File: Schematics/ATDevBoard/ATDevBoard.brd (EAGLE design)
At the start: 67.7 x 54.4 mm, 39 parts, among them U1 TINY85-DIP

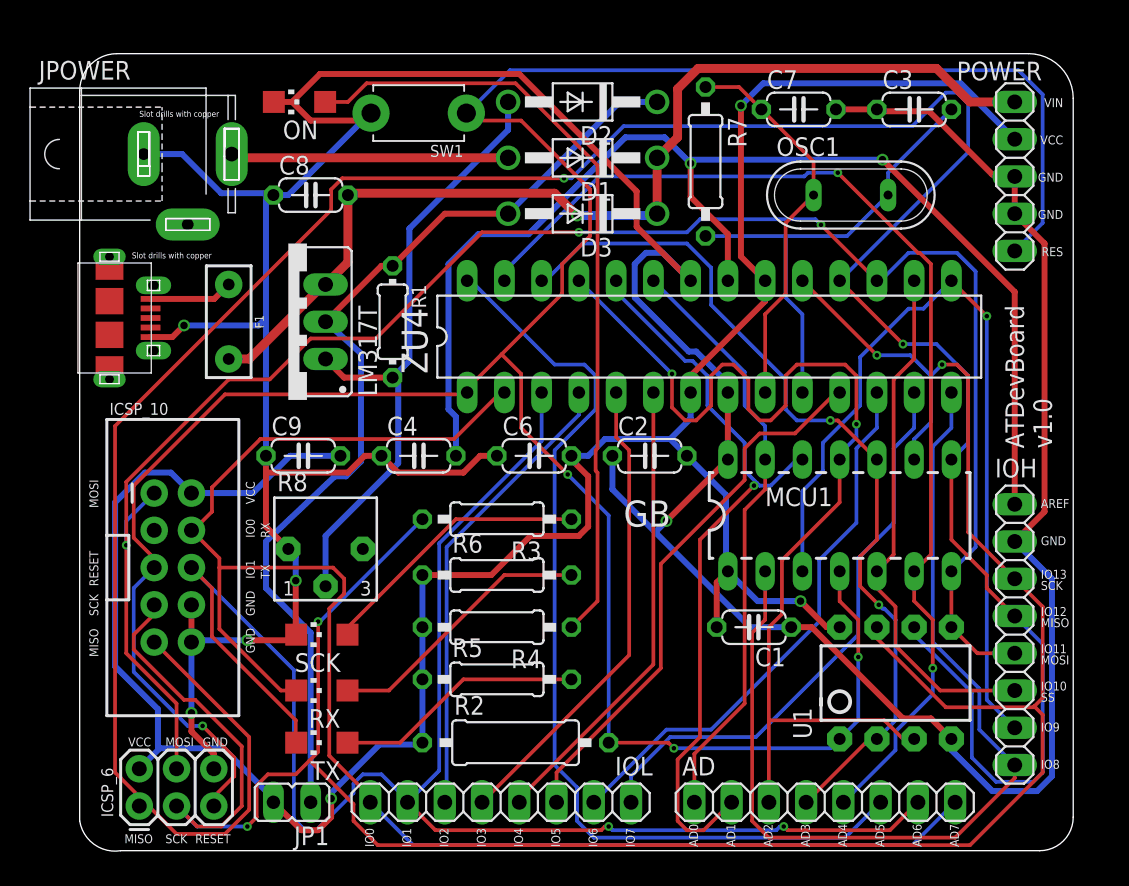
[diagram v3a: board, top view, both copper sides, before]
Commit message: Added fist version of gerber file for SeeedStudio
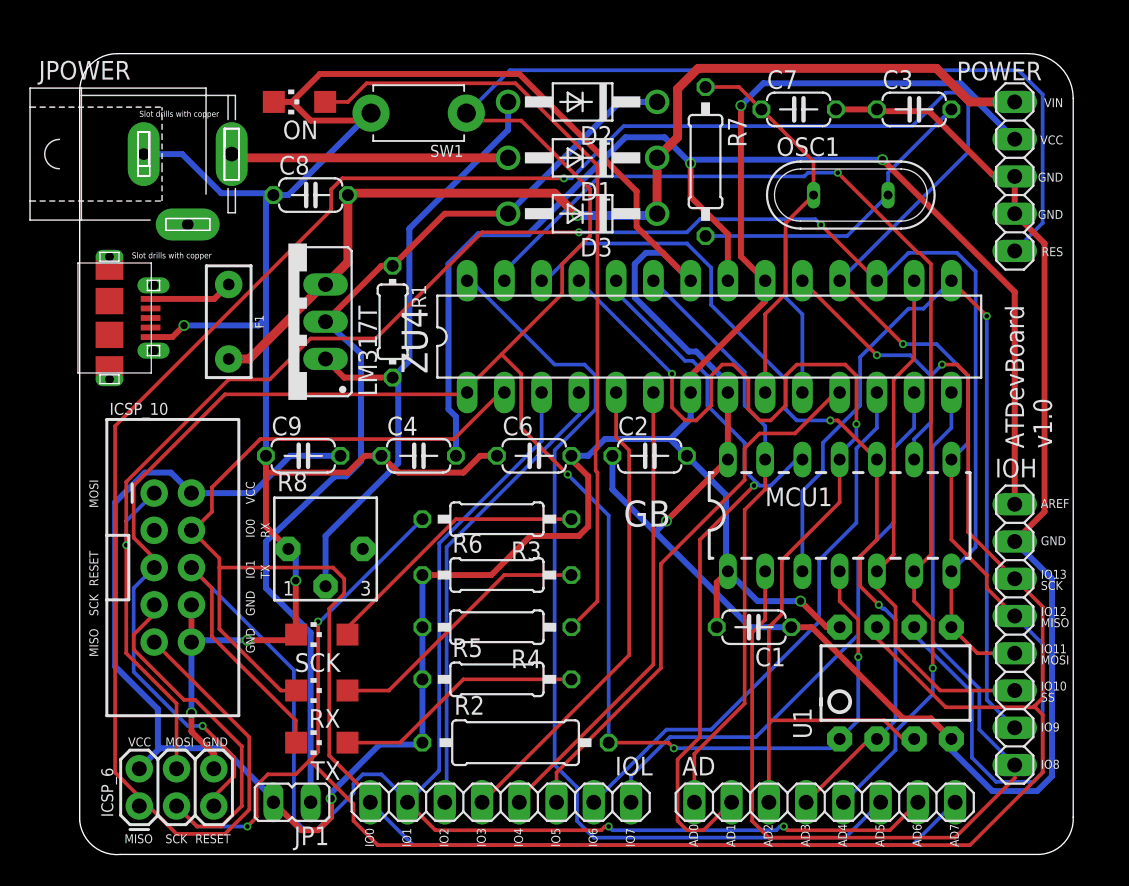
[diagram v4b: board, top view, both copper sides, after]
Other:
- board size 67.7 x 54.4 mm -> 67.7 x 54.6 mm
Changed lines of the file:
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@@
 <plain>
 <wire x1="-0.254" y1="51.298" x2="-0.254" y2="1.524" width="0" layer="20"/>
-<wire x1="-0.254" y1="1.524" x2="2.54" y2="-0.508" width="0" layer="20" curve="90"/>
-<wire x1="2.54" y1="-0.508" x2="65.202" y2="-0.508" width="0" layer="20"/>
-<wire x1="65.202" y1="-0.508" x2="67.488" y2="1.778" width="0" layer="20" curve="90"/>
+<wire x1="-0.254" y1="1.524" x2="2.54" y2="-0.762" width="0" layer="20" curve="90"/>
+<wire x1="2.54" y1="-0.762" x2="65.202" y2="-0.762" width="0" layer="20"/>
+<wire x1="65.202" y1="-0.762" x2="67.488" y2="1.778" width="0" layer="20" curve="90"/>
 <wire x1="67.488" y1="1.778" x2="67.488" y2="50.786046875" width="0" layer="20"/>
 <wire x1="67.488" y1="50.786046875" x2="64.436046875" y2="53.838" width="0" layer="20" curve="90"/>
@@
 </class>
 </classes>
-<designrules name="SeeedStudio_2layer_DRU_no_angle_20140221">
-<description language="de">&lt;b&gt;EAGLE Design Rules&lt;/b&gt;
+<designrules name="oshpark-2layer">
+<description language="en">&lt;b&gt;OSH Park Design Rules&lt;/b&gt;
 &lt;p&gt;
-Die Standard-Design-Rules sind so gewählt, dass sie für
-die meisten Anwendungen passen. Sollte ihre Platine
-besondere Anforderungen haben, treffen Sie die erforderlichen
-Einstellungen hier und speichern die Design Rules unter
-einem neuen Namen ab.</description>
-<description language="en">&lt;b&gt;EAGLE Design Rules&lt;/b&gt;
+Please make sure your boards conform to these design rules.
+&lt;/p&gt;
 &lt;p&gt;
-The default Design Rules have been set to cover
-a wide range of applications. Your particular design
-may have different requirements, so please make the
-necessary adjustments and save your customized
-design rules under a new name.</description>
-<description language="zh">&lt;b&gt;Seeed Studio EAGLE Design Rules&lt;/b&gt;
-</description>
+Note, that not all DRC settings must be set by the manufacturer. Several can be adjusted for the design, including those listed on our docs page here.
+&lt;a href=&quot;http://docs.oshpark.com/design-tools/eagle/design-rules-files/&quot;&gt;Adjustable Settings&lt;/a&gt;
+&lt;/p&gt;</description>
 <param name="layerSetup" value="(1*16)"/>
-<param name="mtCopper" value="0.035mm 0.0175mm 0.035mm 0.035mm 0.035mm 0.035mm 0.035mm 0.035mm 0.035mm 0.035mm 0.035mm 0.035mm 0.035mm 0.035mm 0.0175mm 0.035mm"/>
-<param name="mtIsolate" value="1.5mm 1.1mm 0.2mm 0.15mm 0.2mm 0.15mm 0.2mm 0.15mm 0.2mm 0.15mm 0.2mm 0.15mm 0.2mm 0.15mm 0.2mm"/>
+<param name="mtCopper" value="0.035559375mm 0.0356mm 0.0356mm 0.0356mm 0.0356mm 0.0356mm 0.0356mm 0.0356mm 0.0356mm 0.0356mm 0.0356mm 0.0356mm 0.0356mm 0.0356mm 0.0356mm 0.035559375mm"/>
+<param name="mtIsolate" value="1.6mm 0.1499mm 0.2007mm 0.1499mm 0.2007mm 0.1499mm 0.2007mm 0.1499mm 0.2007mm 0.1499mm 0.2007mm 0.1499mm 0.2007mm 0.1499mm 0.2007mm"/>
 <param name="mdWireWire" value="6mil"/>
 <param name="mdWirePad" value="6mil"/>
@@
 <param name="mdPadVia" value="6mil"/>
 <param name="mdViaVia" value="6mil"/>
-<param name="mdSmdPad" value="0mil"/>
-<param name="mdSmdVia" value="0mil"/>
-<param name="mdSmdSmd" value="0mil"/>
+<param name="mdSmdPad" value="6mil"/>
+<param name="mdSmdVia" value="6mil"/>
+<param name="mdSmdSmd" value="6mil"/>
 <param name="mdViaViaSameLayer" value="8mil"/>
 <param name="mnLayersViaInSmd" value="2"/>
-<param name="mdCopperDimension" value="10mil"/>
-<param name="mdDrill" value="10mil"/>
+<param name="mdCopperDimension" value="15mil"/>
+<param name="mdDrill" value="6mil"/>
 <param name="mdSmdStop" value="0mil"/>
 <param name="msWidth" value="6mil"/>
-<param name="msDrill" value="12mil"/>
-<param name="msMicroVia" value="12mil"/>
+<param name="msDrill" value="10mil"/>
+<param name="msMicroVia" value="10mil"/>
 <param name="msBlindViaRatio" value="0.5"/>
 <param name="rvPadTop" value="0.25"/>
@@
 <param name="rvMicroViaOuter" value="0.25"/>
 <param name="rvMicroViaInner" value="0.25"/>
-<param name="rlMinPadTop" value="10mil"/>
+<param name="rlMinPadTop" value="5mil"/>
 <param name="rlMaxPadTop" value="20mil"/>
-<param name="rlMinPadInner" value="10mil"/>
+<param name="rlMinPadInner" value="5mil"/>
 <param name="rlMaxPadInner" value="20mil"/>
-<param name="rlMinPadBottom" value="10mil"/>
+<param name="rlMinPadBottom" value="5mil"/>
 <param name="rlMaxPadBottom" value="20mil"/>
-<param name="rlMinViaOuter" value="6mil"/>
+<param name="rlMinViaOuter" value="5mil"/>
 <param name="rlMaxViaOuter" value="20mil"/>
-<param name="rlMinViaInner" value="6mil"/>
+<param name="rlMinViaInner" value="5mil"/>
 <param name="rlMaxViaInner" value="20mil"/>
-<param name="rlMinMicroViaOuter" value="4mil"/>
+<param name="rlMinMicroViaOuter" value="5mil"/>
 <param name="rlMaxMicroViaOuter" value="20mil"/>
-<param name="rlMinMicroViaInner" value="4mil"/>
+<param name="rlMinMicroViaInner" value="5mil"/>
 <param name="rlMaxMicroViaInner" value="20mil"/>
 <param name="psTop" value="-1"/>
 <param name="psBottom" value="-1"/>
-<param name="psFirst" value="0"/>
+<param name="psFirst" value="-1"/>
 <param name="psElongationLong" value="100"/>
 <param name="psElongationOffset" value="100"/>
 <param name="mvStopFrame" value="1"/>
 <param name="mvCreamFrame" value="0"/>
-<param name="mlMinStopFrame" value="2mil"/>
-<param name="mlMaxStopFrame" value="2mil"/>
+<param name="mlMinStopFrame" value="2.5mil"/>
+<param name="mlMaxStopFrame" value="2.5mil"/>
 <param name="mlMinCreamFrame" value="0mil"/>
 <param name="mlMaxCreamFrame" value="0mil"/>
-<param name="mlViaStopLimit" value="100mil"/>
+<param name="mlViaStopLimit" value="0mil"/>
 <param name="srRoundness" value="0"/>
 <param name="srMinRoundness" value="0mil"/>
@@
 <param name="checkAngle" value="0"/>
 <param name="checkFont" value="1"/>
-<param name="checkRestrict" value="0"/>
+<param name="checkRestrict" value="1"/>
 <param name="useDiameter" value="13"/>
 <param name="maxErrors" value="50"/>

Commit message: Modified cutout slots for DC connector and micro USB, reviewed name texts in tNames level. Made gerber file for board v1.0, ready for SeeedStudio
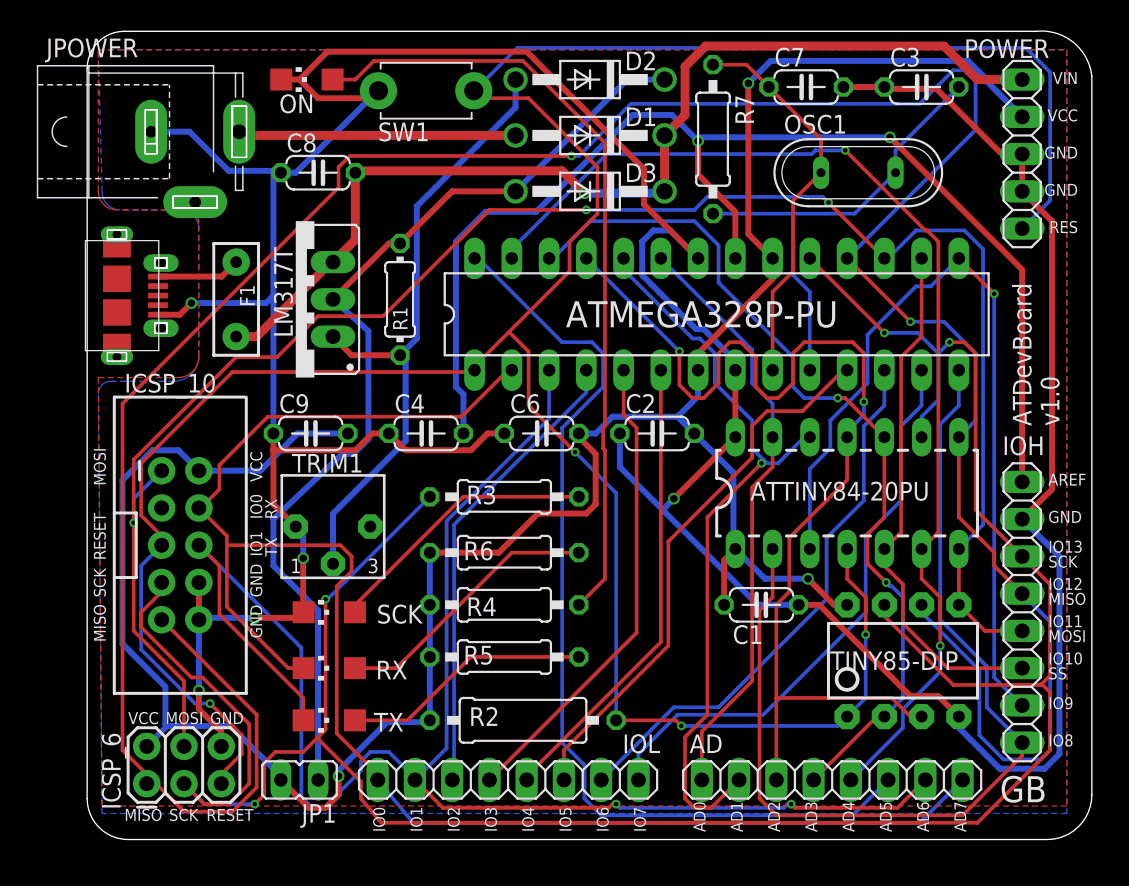
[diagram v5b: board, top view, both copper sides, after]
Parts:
- removed R8: 2K, bourns:3362R
- added TRIM1: 2K, bourns:3362R
- USB1: device con-molex-usb:47589-0001 -> CuSTOM_GB:47589-0001
- moved C1 1.61 mm to (46.2, 16.3)
- moved C2 1.61 mm to (39.1, 27.9)
- moved C7 1.61 mm to (49.3, 51.6)
- moved MCU1 1.61 mm to (53.3, 23.9)
- moved OSC1 1.61 mm to (52.8, 45.7)
- moved R3 1.61 mm to (28.7, 23.6)
- moved R4 1.61 mm to (28.7, 16.3)
- moved R6 1.61 mm to (28.7, 19.8)
- moved R7 1.61 mm to (42.9, 48.0)
- moved ZU4 1.61 mm to (43.2, 36.1)
- moved ON 1.61 mm to (15.2, 52.1)
- moved ICSP_10 1.61 mm to (6.60, 20.3)
- moved JPOWER 1.61 mm to (7.62, 48.5)
- moved R2 1.61 mm to (30.0, 8.38)
- moved USB1 1.61 mm to (2.29, 37.3)
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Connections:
- net GND: now also TRIM1.1; no longer R8.1
- net N$1: now also TRIM1.2; no longer R8.2
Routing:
- added copper zone on layer 1, net GND
- added copper zone on layer 16, net GND
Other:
- board size 67.7 x 54.6 mm -> 68.5 x 55.1 mm
- board text removed: "Slot drills with copper"
